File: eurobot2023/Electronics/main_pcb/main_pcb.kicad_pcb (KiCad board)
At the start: 2 copper layers, 65.3 x 90.9 mm, 4 parts, among them J1 PI40HAT, J2 Conn_01x03, Q1 BSH108,215, U1 PCA9517AD

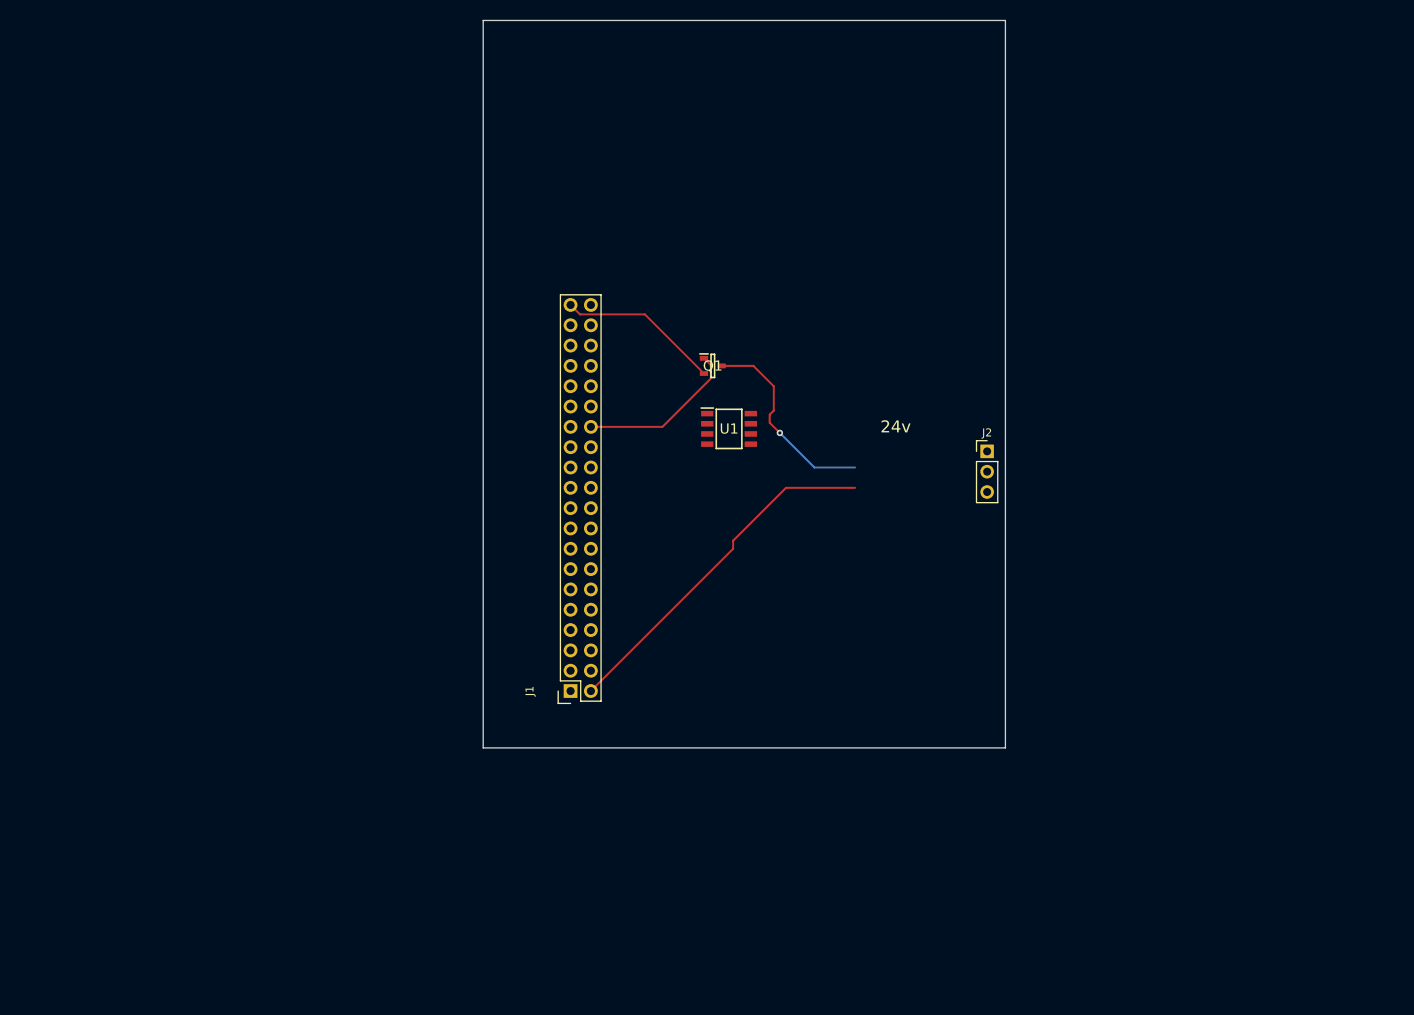
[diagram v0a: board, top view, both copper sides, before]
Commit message: Electronics: partial draft of PCB.
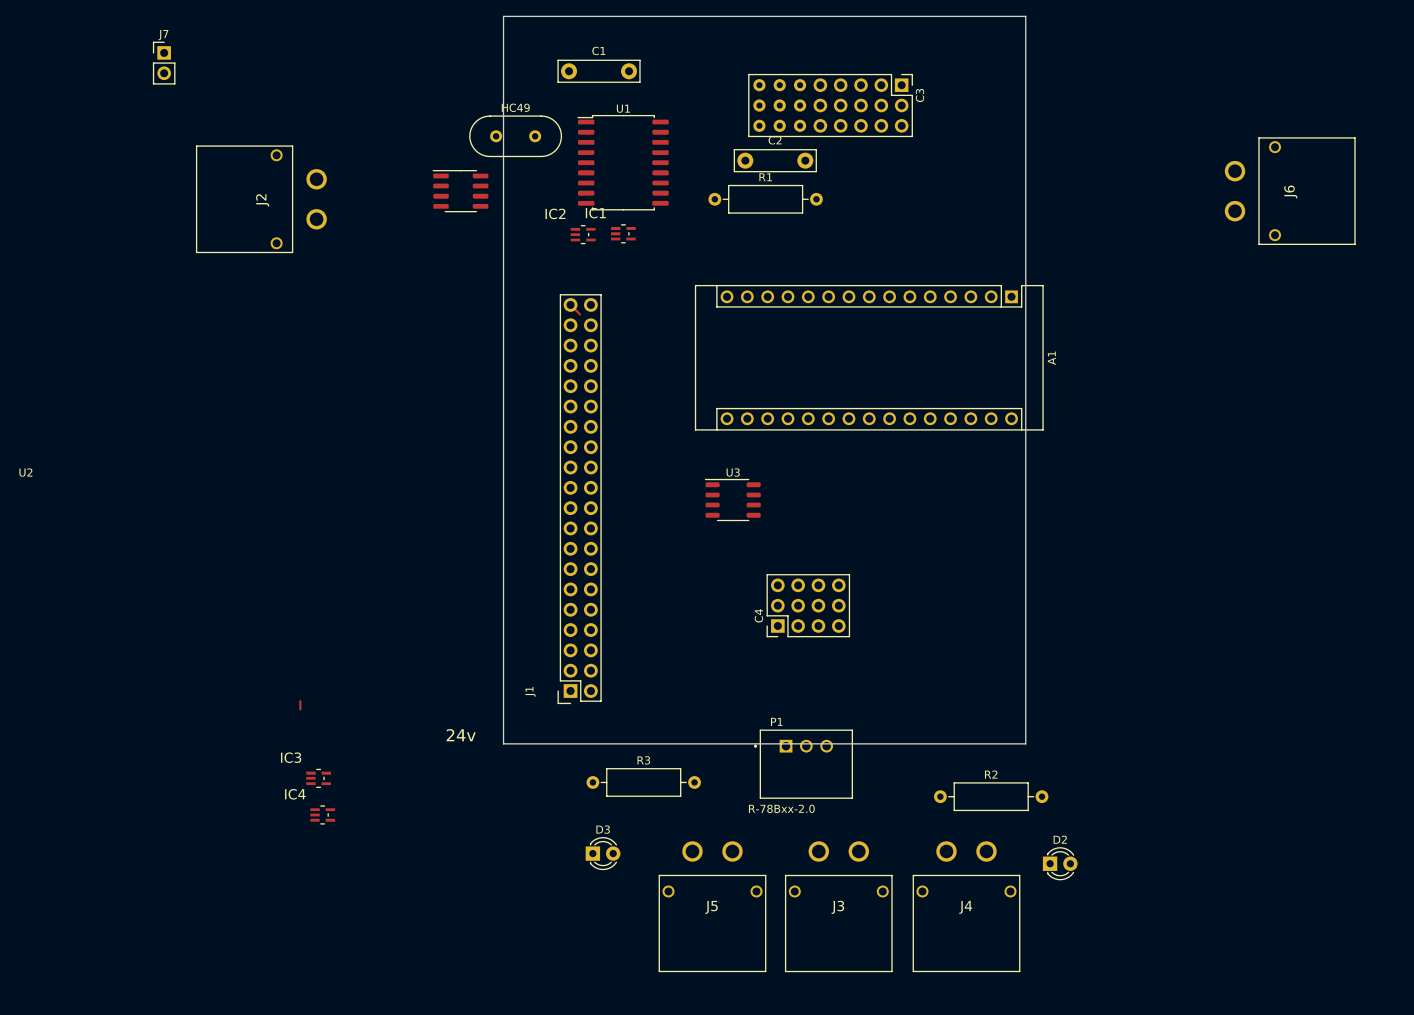
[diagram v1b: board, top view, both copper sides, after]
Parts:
- removed Q1: BSH108,215, MiAM:SOT95P230X110-3N
- added A1: Arduino_Nano_Every, Module:Arduino_Nano, F.Cu at (136.4, 62.5)
- added C1: C, Capacitor_THT:C_Rect_L10.0mm_W2.5mm_P7.50mm_MKS4, F.Cu at (81.1, 34.3)
- added C2: C, Capacitor_THT:C_Rect_L10.0mm_W2.5mm_P7.50mm_MKS4, F.Cu at (103.1, 45.5)
- added C3: Conn_03x08, MiAM:Pin_Header_Straight_3x08_Pitch2.54mm, F.Cu at (122.7, 36.0)
- added C4: Conn_03x04, MiAM:Pin_Header_Straight_3x04_Pitch2.54mm, F.Cu at (107.2, 103.6)
- added D2: LED, LED_THT:LED_D3.0mm, F.Cu at (141.2, 133.3)
- added D3: LED, LED_THT:LED_D3.0mm, F.Cu at (84.1, 132.1)
- added HC49: Crystal, Crystal:Crystal_HC49-4H_Vertical, F.Cu at (72.0, 42.4)
- added IC1: 74HCT1G125GW, MiAM:SOT65P210X110-5N, F.Cu at (87.9, 54.6)
- added IC2: 74HCT1G125GW, MiAM:SOT65P210X110-5N, F.Cu at (82.9, 54.7)
- added IC3: 74HCT1G125GW, MiAM:SOT65P210X110-5N, F.Cu at (49.8, 122.7)
- added IC4: 74HCT1G125GW, MiAM:SOT65P210X110-5N, F.Cu at (50.3, 127.3)
- added J3: Conn_01x02_Male, MiAM:XT30PWF, F.Cu at (117.3, 131.8)
- added J4: Conn_01x02_Male, MiAM:XT30PWF, F.Cu at (133.3, 131.8)
- added J5: Conn_01x02_Male, MiAM:XT30PWF, F.Cu at (101.5, 131.8)
- added J6: Conn_01x02_Male, MiAM:XT30PWF, F.Cu at (164.3, 46.8)
- added J7: Conn_01x02_Male, Connector_PinHeader_2.54mm:PinHeader_1x02_P2.54mm_Vertical, F.Cu at (30.5, 32.0)
- added P1: R-78Bxx-2.0, MiAM:CONV_R-78Bxx-2.0, F.Cu at (108.2, 118.7)
- added R1: 10k, Resistor_THT:R_Axial_DIN0309_L9.0mm_D3.2mm_P12.70mm_Horizontal, F.Cu at (99.3, 50.3)
- added R2: R, Resistor_THT:R_Axial_DIN0309_L9.0mm_D3.2mm_P12.70mm_Horizontal, F.Cu at (127.5, 125.0)
- added R3: R, Resistor_THT:R_Axial_DIN0309_L9.0mm_D3.2mm_P12.70mm_Horizontal, F.Cu at (84.1, 123.2)
- added U2: TJA1049T, Package_SO:SOIC-8_3.9x4.9mm_P1.27mm, F.Cu at (67.6, 49.3)
- added U3: PCA9306D, Package_SO:SO-8_3.9x4.9mm_P1.27mm, F.Cu at (101.6, 87.9)
- J2: value Conn_01x03 -> Conn_01x02_Male; footprint Connector_PinHeader_2.54mm:PinHeader_1x03_P2.54mm_Vertical -> MiAM:XT30PWF
- U1: value PCA9517AD -> MCP2515-xSO; footprint MiAM:SOIC127P600X175-8N -> Package_SO:SOIC-18W_7.5x11.6mm_P1.27mm
- moved J2 88.7 mm to (49.5, 52.8), turned to 90 degrees
- moved U1 35.8 mm to (87.9, 45.7)
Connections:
- J1 pad 1: unconnected-(J1-Pad1) -> +3.3V
- J1 pad 28: Net-(J1-Pad28) -> unconnected-(J1-Pad28)
- J1 pad 3: unconnected-(J1-Pad3) -> /I2C SDA
- J1 pad 35: unconnected-(J1-Pad35) -> /SPI1 MISO
- J1 pad 36: unconnected-(J1-Pad36) -> /SPI1 CS2
- J1 pad 38: unconnected-(J1-Pad38) -> /SPI1 MOSI
- J1 pad 40: unconnected-(J1-Pad40) -> /SPI1 CLK
- J1 pad 5: unconnected-(J1-Pad5) -> /I2C SCL
- J2 pad 2: Net-(J2-Pad2) -> GND
- J2 pad 3: +5V -> (no net)
- U1 pad 1: unconnected-(U1-Pad1) -> Net-(U2-Pad1)
- U1 pad 2: unconnected-(U1-Pad2) -> Net-(U2-Pad4)
- U1 pad 7: unconnected-(U1-Pad7) -> Net-(HC49-Pad2)
- U1 pad 8: unconnected-(U1-Pad8) -> Net-(C2-Pad2)
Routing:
- net +5V: track 44.1 -> 1.02 mm
- net Net-(J2-Pad2): track 25.3 -> 0.00 mm, vias 1 -> 0
- net Net-(J1-Pad28): track 20.4 -> 0.00 mm
- net GND: track 20.2 -> 1.68 mm

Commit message: [eurobot2023/Electronics] Continue schematic
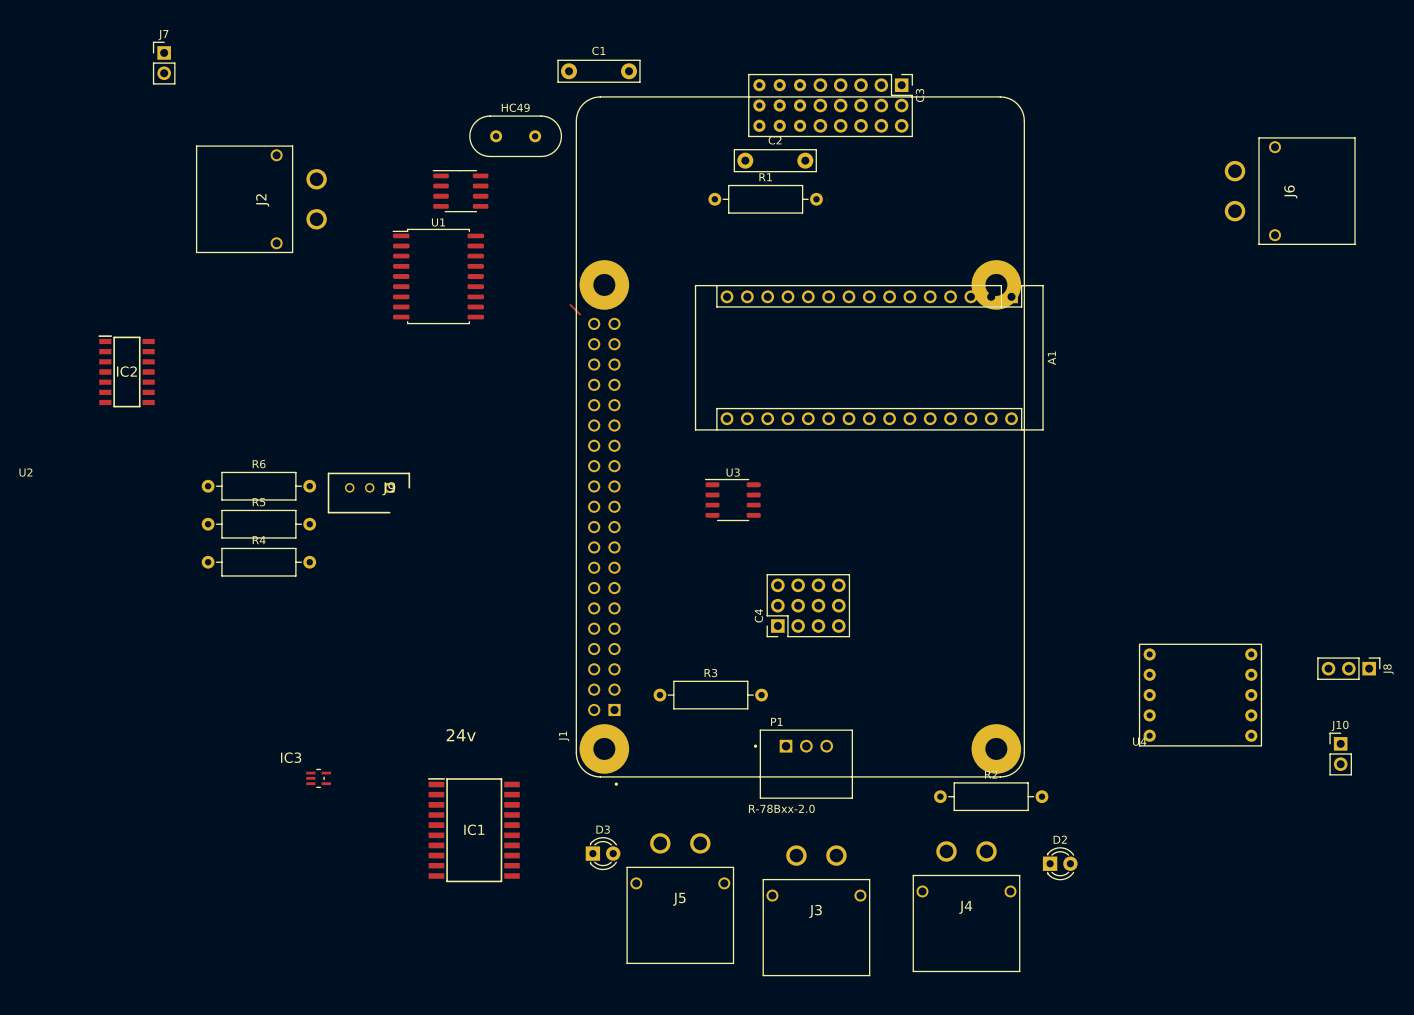
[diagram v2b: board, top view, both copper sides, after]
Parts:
- removed IC4: 74HCT1G125GW, MiAM:SOT65P210X110-5N
- added J10: Conn_01x02_Male, Connector_PinHeader_2.54mm:PinHeader_1x02_P2.54mm_Vertical, F.Cu at (177.5, 118.4)
- added J8: Conn_01x03_Male, Connector_PinHeader_2.54mm:PinHeader_1x03_P2.54mm_Vertical, F.Cu at (181.1, 109.0)
- added J9: 22-03-5035, MiAM:SHDR3W60P0X250_1X3_990X490X590P, F.Cu at (58.7, 86.4)
- added R4: 10k, Resistor_THT:R_Axial_DIN0309_L9.0mm_D3.2mm_P12.70mm_Horizontal, F.Cu at (36.0, 95.7)
- added R5: 10k, Resistor_THT:R_Axial_DIN0309_L9.0mm_D3.2mm_P12.70mm_Horizontal, F.Cu at (36.0, 90.9)
- added R6: 10k, Resistor_THT:R_Axial_DIN0309_L9.0mm_D3.2mm_P12.70mm_Horizontal, F.Cu at (36.0, 86.2)
- added U4: Pololu_MAX14870, MiAM:PololuMAX14870, F.Cu at (152.4, 118.6)
- IC1: value 74HCT1G125GW -> 74HCT541D,652; footprint MiAM:SOT65P210X110-5N -> MiAM:SOIC127P1032X265-20N
- IC2: value 74HCT1G125GW -> SN74LVC126ADR; footprint MiAM:SOT65P210X110-5N -> MiAM:SOIC127P600X175-14N
- J1: footprint MiAM:Socket_Strip_Straight_2x20 -> MiAM:MODULE_RASPBERRY_PI_B+
- moved IC1 76.8 mm to (69.2, 129.2)
- moved IC2 59.6 mm to (25.8, 71.9)
- moved J1 42.8 mm to (110.0, 80.0)
- moved U1 27.1 mm to (64.8, 59.9)
- moved R3 13.8 mm to (92.5, 112.3)
- moved J5 4.15 mm to (97.5, 130.8)
- moved J3 2.84 mm to (114.5, 132.3)
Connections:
- IC1 pad 2: /SPI1 CS2 -> /SPI1_CS0
- IC1 pad 3: GND -> /SPI1_CS1
- IC1 pad 4: Net-(IC1-Pad4) -> /SPI1 CS2
- IC1 pad 5: +5V -> /SPI1 MOSI
- IC2 pad 1: GND -> +3.3V
- IC2 pad 2: /SPI1 MOSI -> /SPI1 MISO_5
- IC2 pad 3: GND -> /SPI1 MISO
- IC2 pad 4: Net-(IC2-Pad4) -> /Servo RX
- IC2 pad 5: +5V -> /UART_RX_5
- IC3 pad 1: GND -> /Servo RX
- IC3 pad 2: /SPI1 CLK -> /UART_TX_5
- IC3 pad 4: Net-(IC3-Pad4) -> /UART_RX_5
- J1 pad 10: unconnected-(J1-Pad10) -> /UART_RX
- J1 pad 11: unconnected-(J1-Pad11) -> /SPI1_CS0
- J1 pad 12: unconnected-(J1-Pad12) -> /SPI1_CS1
- J1 pad 16: unconnected-(J1-Pad16) -> /Servo RX
- J1 pad 4: unconnected-(J1-Pad4) -> +5V
- J1 pad 8: unconnected-(J1-Pad8) -> /UART_TX
- U1 pad 13: Net-(IC3-Pad4) -> /SPI1 CLK_5
- U1 pad 14: Net-(IC2-Pad4) -> /SPI1 MOSI_5
- U1 pad 15: Net-(IC4-Pad2) -> /SPI1 MISO_5
- U1 pad 16: Net-(IC1-Pad4) -> /SPI1_CS0_5
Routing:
- net +5V: track 1.02 -> 0.00 mm
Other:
- board outline removed

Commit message: [miam_utils] Add driver for the AS5045 magnetic encoder.
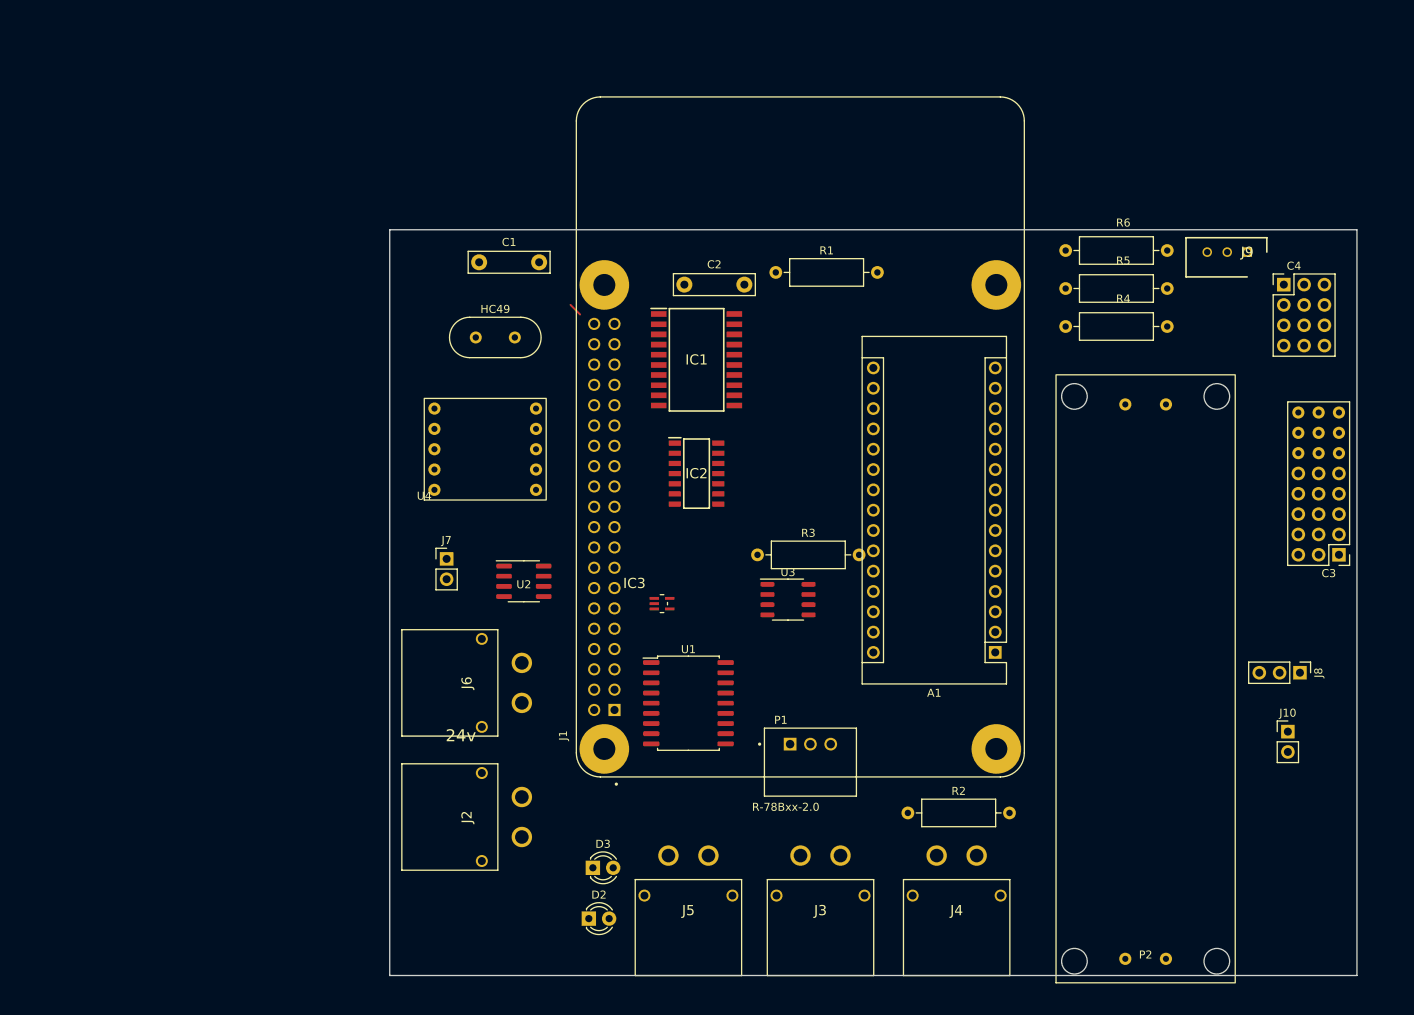
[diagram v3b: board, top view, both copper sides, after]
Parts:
- added P2: Amazon 10A stepdown, MiAM:StepDown10A, F.Cu at (153.2, 145.2)
- moved J6 111.2 mm to (75.2, 113.2), turned to 90 degrees
- moved R4 111.2 mm to (143.2, 66.2)
- moved R5 111.2 mm to (143.2, 61.4)
- moved R6 111.2 mm to (143.2, 56.7)
- moved J9 111.2 mm to (165.9, 56.9)
- moved U4 94.5 mm to (63.0, 87.9)
- moved J2 81.4 mm to (75.2, 130.0)
- moved C3 80.2 mm to (177.3, 94.7), turned to 180 degrees
- moved C4 76.3 mm to (170.4, 61.0), turned to 0 degrees
- moved J7 72.4 mm to (65.8, 95.2)
- moved IC2 72.3 mm to (97.0, 84.6)
- moved IC1 65.0 mm to (97.0, 70.4)
- moved U1 61.8 mm to (96.0, 113.3)
- moved D2 58.1 mm to (83.6, 140.2)
- moved U2 49.4 mm to (75.4, 98.0)
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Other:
- board outline added: 120.9 x 93.2 mm

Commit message: PDB update.
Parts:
- added J11: MagneticEncoder, MiAM:52746-0671, F.Cu at (45.0, 116.6)
- J2, J3, J4, J5, J6: footprint MiAM:XT30PWF -> MiAM:XT30UM
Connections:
- J2 pad 1: +24V -> Net-(J2-Pad1)
- J2 pad 2: GND -> Net-(J4-Pad1)
- J3 pad 1: Net-(J3-Pad1) -> Net-(J2-Pad1)
- J3 pad 2: Net-(J3-Pad2) -> GND
- J4 pad 1: Net-(J3-Pad2) -> Net-(J4-Pad1)
- J5 pad 1: Net-(J3-Pad1) -> +24V
- P1 pad 1: Net-(J3-Pad2) -> Net-(J4-Pad1)
- R3 pad 2: Net-(J3-Pad2) -> Net-(J4-Pad1)
- U3 pad 2: +5V -> +3.3V
- U3 pad 7: +3.3V -> +5V

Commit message: Update pcb
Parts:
- removed A1: Arduino_Nano_Every, Module:Arduino_Nano
- removed J8: Conn_01x03_Male, Connector_PinHeader_2.54mm:PinHeader_1x03_P2.54mm_Vertical
- added J12: Conn_01x07_Male, Connector_PinHeader_2.54mm:PinHeader_1x07_P2.54mm_Vertical, F.Cu at (68.6, 72.8)
- added J13: MagneticEncoder, MiAM:52746-0671, F.Cu at (178.9, 140.3)
- added J14: Conn_01x03_Male, Connector_PinHeader_2.54mm:PinHeader_1x03_P2.54mm_Vertical, F.Cu at (132.1, 88.1)
- added J15: Conn_01x02_Male, Connector_PinHeader_2.54mm:PinHeader_1x02_P2.54mm_Vertical, F.Cu at (180.3, 123.6)
- added U5: PCA9685PW, Package_SO:TSSOP-28_4.4x9.7mm_P0.65mm, F.Cu at (134.6, 77.9)
- moved C4 106.1 mm to (71.1, 98.2)
- moved U4 106.0 mm to (168.9, 90.6), turned to -90 degrees
- moved J6 101.5 mm to (172.7, 141.4)
- moved R4 77.2 mm to (66.0, 63.5)
- moved HC49 76.1 mm to (119.4, 125.0)
- moved C1 72.2 mm to (118.2, 111.8)
- moved C2 60.8 mm to (118.2, 117.3)
- moved D2 48.7 mm to (132.1, 136.3)
- moved J2 46.3 mm to (119.4, 144.0), turned to 180 degrees
- moved R2 38.6 mm to (90.2, 146.5), turned to 180 degrees
- moved U2 38.2 mm to (88.9, 133.8)
- moved D3 32.9 mm to (116.8, 136.3)
- moved J11 32.5 mm to (68.6, 138.9), turned to -90 degrees
- moved J7 28.5 mm to (68.6, 123.6)
- moved J5 24.1 mm to (76.2, 141.4), turned to 90 degrees
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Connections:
- C3 pad 1: unconnected-(C3-Pad1) -> GND
- C3 pad 10: unconnected-(C3-Pad10) -> GND
- C3 pad 11: unconnected-(C3-Pad11) -> +7.5V
- C3 pad 13: unconnected-(C3-Pad13) -> GND
- C3 pad 14: unconnected-(C3-Pad14) -> +7.5V
- C3 pad 16: unconnected-(C3-Pad16) -> GND
- C3 pad 17: unconnected-(C3-Pad17) -> +7.5V
- C3 pad 19: unconnected-(C3-Pad19) -> GND
- C3 pad 2: unconnected-(C3-Pad2) -> +7.5V
- C3 pad 20: unconnected-(C3-Pad20) -> +7.5V
- C3 pad 22: unconnected-(C3-Pad22) -> GND
- C3 pad 23: unconnected-(C3-Pad23) -> +7.5V
- C3 pad 4: unconnected-(C3-Pad4) -> GND
- C3 pad 5: unconnected-(C3-Pad5) -> +7.5V
- C3 pad 7: unconnected-(C3-Pad7) -> GND
- C3 pad 8: unconnected-(C3-Pad8) -> +7.5V
- C4 pad 11: +5V -> +3.3V
- C4 pad 12: Net-(A1-Pad22) -> /GPIO 23
- C4 pad 2: +5V -> +3.3V
- C4 pad 3: Net-(A1-Pad19) -> /GPIO 20
- C4 pad 5: +5V -> +3.3V
- C4 pad 6: Net-(A1-Pad20) -> /GPIO 21
- C4 pad 8: +5V -> +3.3V
- C4 pad 9: Net-(A1-Pad21) -> /GPIO 22
- J1 pad 11: /SPI1_CS0 -> unconnected-(J1-Pad11)
- J1 pad 12: /SPI1_CS1 -> /Servo RX
- J1 pad 15: unconnected-(J1-Pad15) -> /GPIO 22
- J1 pad 16: /Servo RX -> /GPIO 23
- J1 pad 19: unconnected-(J1-Pad19) -> /SPI1 MOSI
- J1 pad 21: unconnected-(J1-Pad21) -> /SPI1 MISO
- J1 pad 23: unconnected-(J1-Pad23) -> /SPI1 CLK
- J1 pad 24: unconnected-(J1-Pad24) -> /SPI1_CS0
- J1 pad 26: unconnected-(J1-Pad26) -> /SPI1_CS1
- J1 pad 29: unconnected-(J1-Pad29) -> /GPIO 5
- J1 pad 31: unconnected-(J1-Pad31) -> /GPIO 6
- J1 pad 32: unconnected-(J1-Pad32) -> /GPIO 12
- J1 pad 35: /SPI1 MISO -> unconnected-(J1-Pad35)
- J1 pad 36: /SPI1 CS2 -> /GPIO 16
- J1 pad 38: /SPI1 MOSI -> /GPIO 20
- J1 pad 40: /SPI1 CLK -> /GPIO 21
- J1 pad 7: unconnected-(J1-Pad7) -> /GPIO 4
- U4 pad 1: unconnected-(U4-Pad1) -> /GPIO 12
- U4 pad 2: unconnected-(U4-Pad2) -> /GPIO 16
- U4 pad 9: Net-(J8-Pad2) -> +7.5V
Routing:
- net GND: track 1.68 -> 0.00 mm
